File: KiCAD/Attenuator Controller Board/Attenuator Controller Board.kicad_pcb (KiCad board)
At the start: 2 copper layers, 100 x 70 mm, 33 parts, among them J1 Barrel_Jack_Switch, J2 Conn_Coaxial, J3 Conn_Coaxial, J4 Conn_01x24_Female, J5 DSub_15_HD, J6 DSub9, J7 DSub9, J8 DSub9, J9 Conn_01x24_Female, U1 ADM3307EARUZ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

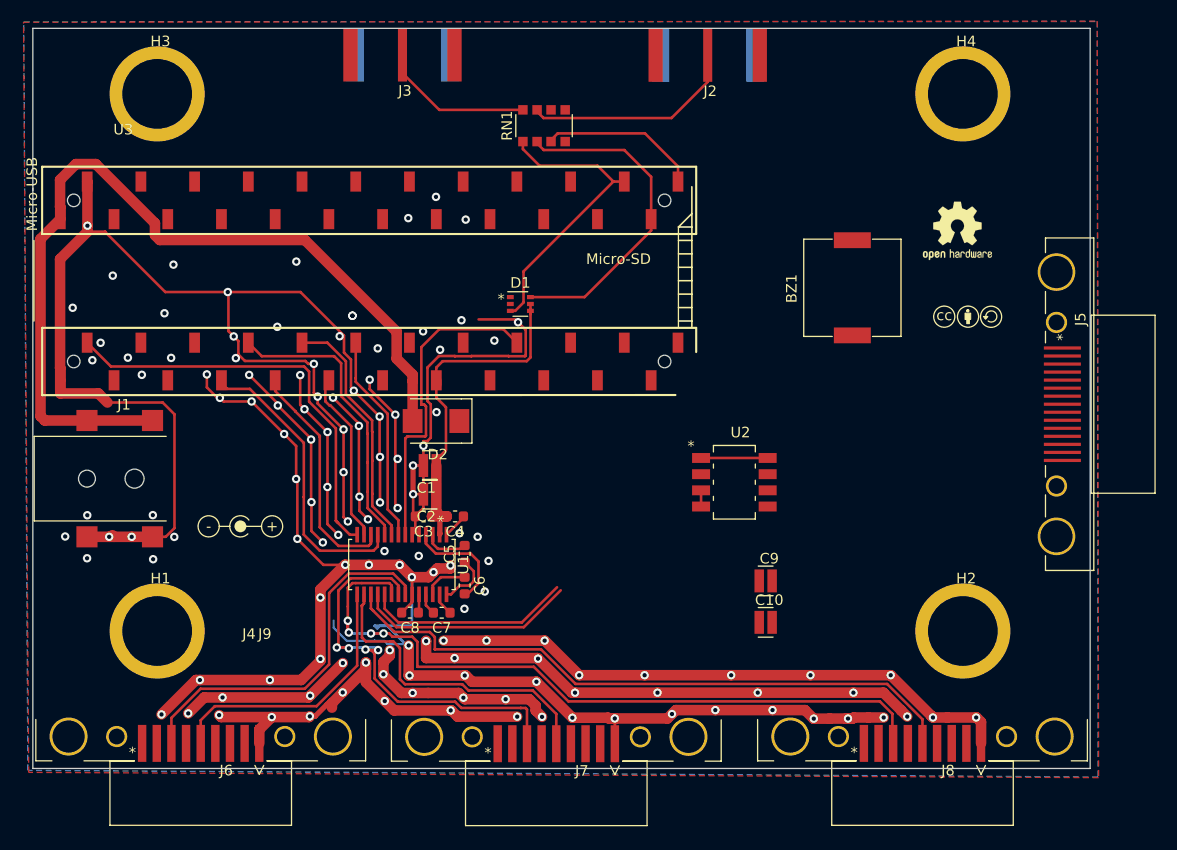
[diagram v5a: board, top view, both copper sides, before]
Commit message: Started on Thorlabs connections
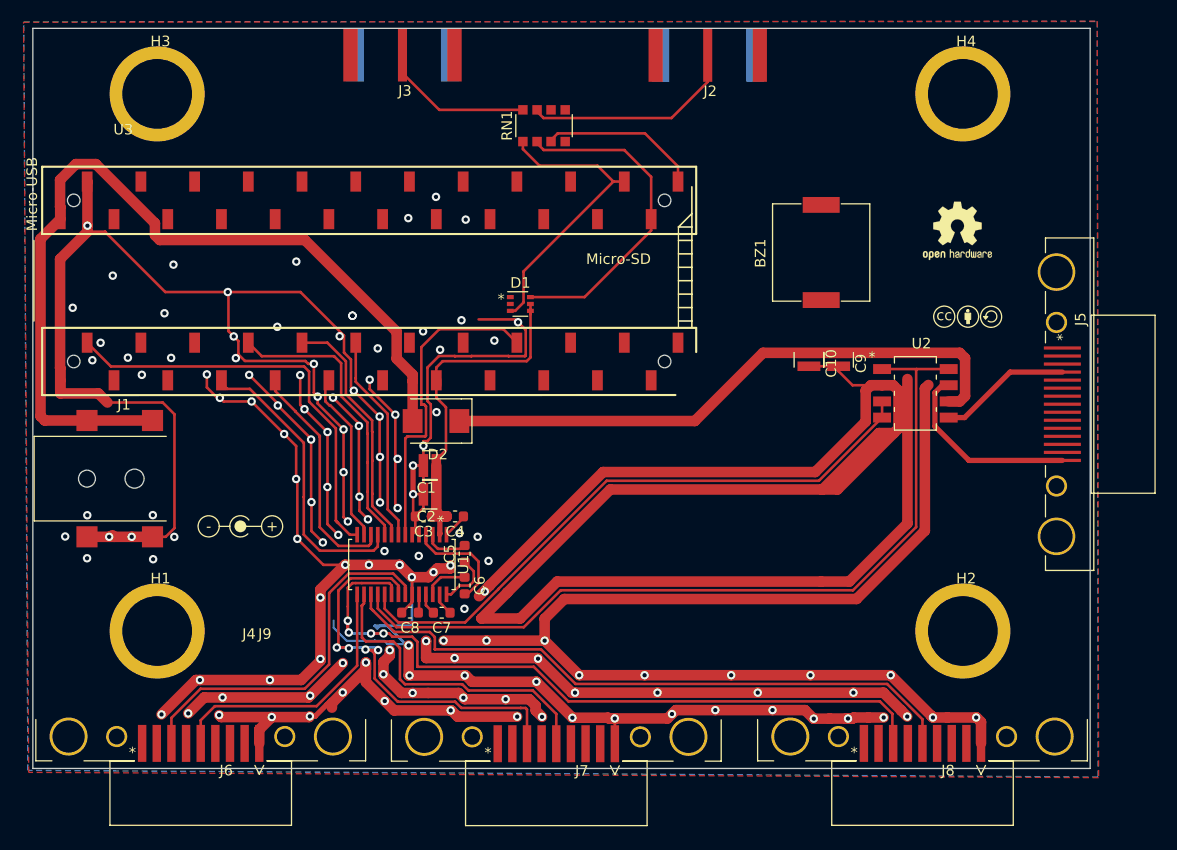
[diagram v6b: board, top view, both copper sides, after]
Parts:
- moved C10 25.2 mm to (173.4, 101.3), turned to 270 degrees
- moved C9 22.0 mm to (176.2, 101.3), turned to 270 degrees
- moved U2 19.1 mm to (183.5, 104.5)
- moved BZ1 4.46 mm to (170.1, 91.2)
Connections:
- U2 pad 5: /Motor(+) -> /Motor(-)
- U2 pad 7: /Motor(-) -> /Motor(+)
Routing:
- net GND: track 552.3 -> 782.7 mm
- net Net-(C10-Pad1): track 0.00 -> 56.1 mm
- net /Gate3-4: track 27.1 -> 78.6 mm
- net /Gate1-2: track 21.1 -> 58.5 mm
- net /Motor(+): track 0.00 -> 18.2 mm
- net /Motor(-): track 0.00 -> 12.5 mm

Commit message: More DSub-15 connections
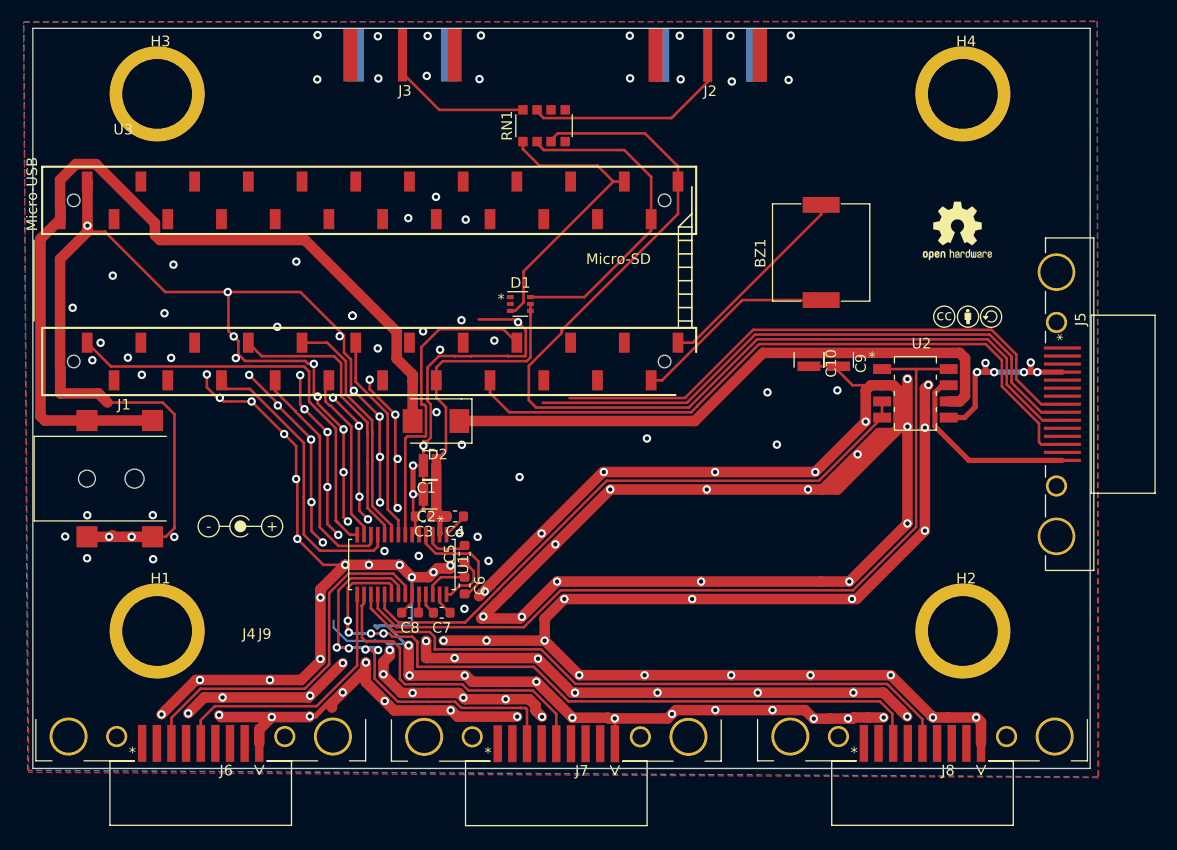
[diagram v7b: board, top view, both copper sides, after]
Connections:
- J5 pad 10: /3v3 -> /Ident-Vcc
- U3 pad 13: /Alarm1 -> Net-(J4-Pad~)
- U3 pad 14: /Alarm2 -> Net-(J4-Pad~)
- U3 pad 17: /NC25 -> /Ident-Vcc
- U3 pad 23: Net-(J4-Pad~) -> /Alarm1
- U3 pad 24: Net-(J4-Pad~) -> /Alarm2
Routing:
- net /Ident(-): track 15.1 -> 99.7 mm
- net /Ident-Vcc: track 0.00 -> 65.2 mm
- net /Limit_Switch: track 0.00 -> 56.3 mm
- net /Encoder(A): track 0.00 -> 53.6 mm
- net /Alarm2: track 0.00 -> 19.5 mm
- net /Alarm1: track 0.00 -> 19.2 mm
- net /Motor(-): track 12.5 -> 20.9 mm, vias 0 -> 6
- net GND: vias 138 -> 184

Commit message: DSub 9 aligned
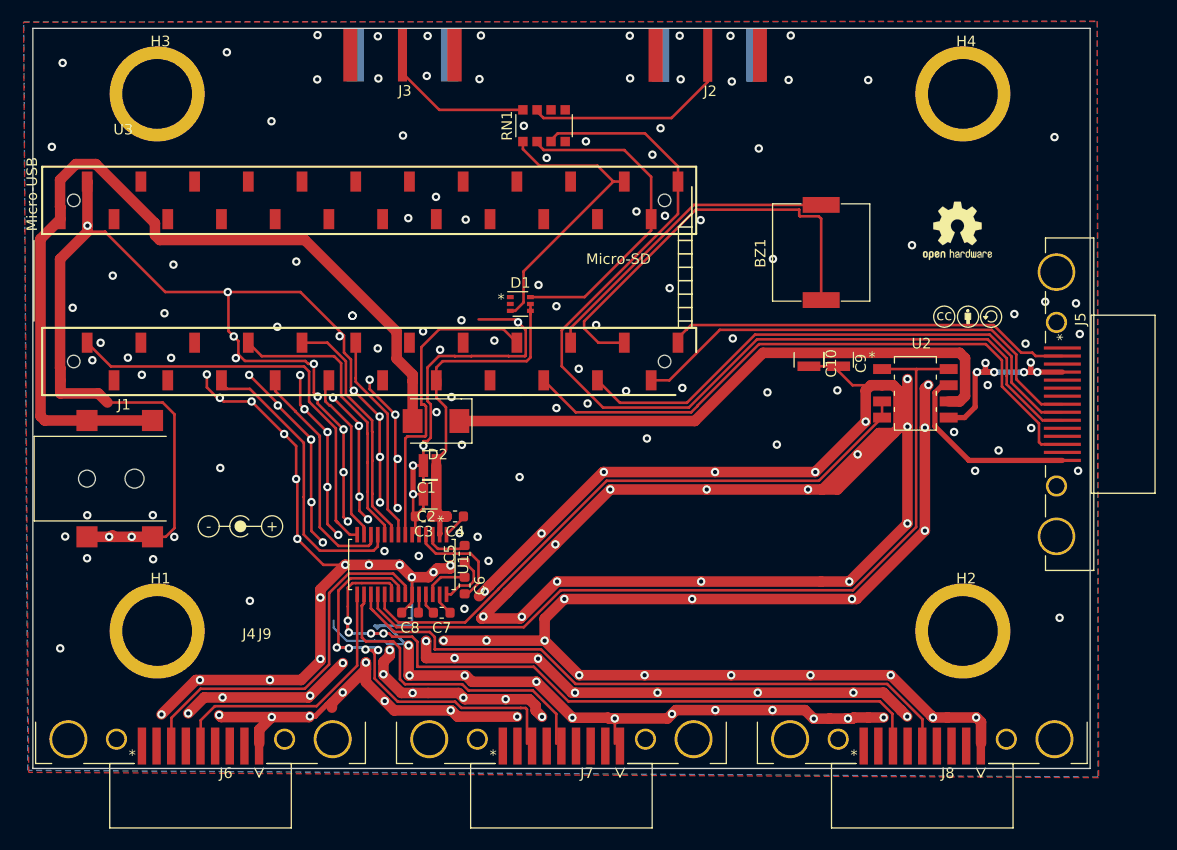
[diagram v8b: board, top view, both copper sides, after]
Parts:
- moved J7 0.53 mm to (150.0, 139.5)
- moved J6 0.25 mm to (115.9, 139.5)
- moved J8 0.25 mm to (184.1, 139.5)
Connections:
- U3 pad 13: Net-(J4-Pad~) -> /NC11
- U3 pad 14: Net-(J4-Pad~) -> /NC12
- U3 pad 17: /Ident-Vcc -> /NC25
- U3 pad 19: /NC27 -> /Ident-Vcc
- U3 pad 20: /NC28 -> /Alarm2
- U3 pad 21: Net-(J4-Pad~) -> /Limit_Switch
- U3 pad 22: Net-(J4-Pad~) -> /Alarm1
- U3 pad 23: /Alarm1 -> /Encoder(A)
- U3 pad 24: /Alarm2 -> /Encoder(B)
- U3 pad 51: /3v3 -> /NC3v3
- U3 pad 6: /Limit_Switch -> /NC4
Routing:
- net /Encoder(B): track 0.00 -> 38.5 mm
- net /Alarm1: track 19.2 -> 40.2 mm
- net /Alarm2: track 19.5 -> 29.9 mm
- net /Encoder(A): track 53.6 -> 45.2 mm
- net /Ident(-): track 99.7 -> 93.4 mm
- net /Ident-Vcc: track 65.2 -> 59.4 mm
- net /Limit_Switch: track 56.3 -> 52.0 mm
- net GND: vias 184 -> 228
